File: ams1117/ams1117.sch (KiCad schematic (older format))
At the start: 8 parts, among them J1 PWR_IN, J2 PWR_OUT, J3 RAW, U1 AMS1117

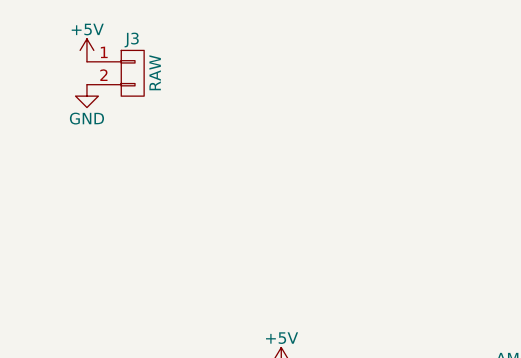
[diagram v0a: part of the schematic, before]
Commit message: 完成AMS1117降压模块PCB绘制
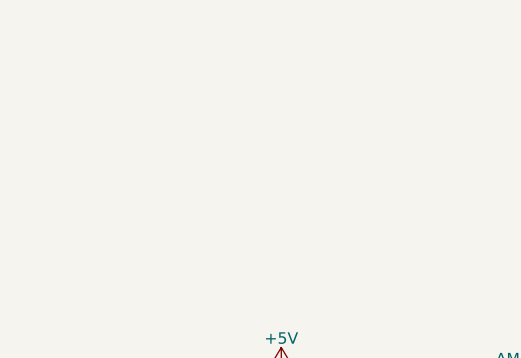
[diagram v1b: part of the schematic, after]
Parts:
- removed J3: RAW, symbol CONN_01X02
- C1, C4: footprint Capacitors_THT:CP_Radial_D5.0mm_P2.50mm -> Capacitors_SMD:CP_Elec_5x5.3
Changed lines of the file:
@@
 LIBS:contrib
 LIBS:valves
-LIBS:tmulin
 LIBS:ams1117-cache
 EELAYER 25 0
@@
 F 0 "C1" H 3175 3950 50  0000 L CNN
 F 1 "22uF" H 3175 3750 50  0000 L CNN
-F 2 "Capacitors_THT:CP_Radial_D5.0mm_P2.50mm" H 3188 3700 50  0001 C CNN
+F 2 "Capacitors_SMD:CP_Elec_5x5.3" H 3188 3700 50  0001 C CNN
 F 3 "" H 3150 3850 50  0001 C CNN
 	1    3150 3850
@@
 F 0 "C4" H 5425 3950 50  0000 L CNN
 F 1 "22uF" H 5425 3750 50  0000 L CNN
-F 2 "Capacitors_THT:CP_Radial_D5.0mm_P2.50mm" H 5438 3700 50  0001 C CNN
+F 2 "Capacitors_SMD:CP_Elec_5x5.3" H 5438 3700 50  0001 C CNN
 F 3 "" H 5400 3850 50  0001 C CNN
 	1    5400 3850
@@
 	1    0    0    -1
 $EndComp
-$Comp
-L CONN_01X02 J3
-U 1 1 5A055310
-P 2500 2100
-F 0 "J3" H 2500 2250 50  0000 C CNN
-F 1 "RAW" V 2600 2100 50  0000 C CNN
-F 2 "" H 2500 2100 50  0001 C CNN
-F 3 "" H 2500 2100 50  0001 C CNN
-	1    2500 2100
-	1    0    0    -1
-$EndComp
-$Comp
-L +5V #PWR010
-U 1 1 5A0553C5
-P 2300 2050
-F 0 "#PWR010" H 2300 1900 50  0001 C CNN
-F 1 "+5V" H 2300 2190 50  0000 C CNN
-F 2 "" H 2300 2050 50  0001 C CNN
-F 3 "" H 2300 2050 50  0001 C CNN
-	1    2300 2050
-	1    0    0    -1
-$EndComp
-$Comp
-L GND #PWR011
-U 1 1 5A0553F9
-P 2300 2150
-F 0 "#PWR011" H 2300 1900 50  0001 C CNN
-F 1 "GND" H 2300 2000 50  0000 C CNN
-F 2 "" H 2300 2150 50  0001 C CNN
-F 3 "" H 2300 2150 50  0001 C CNN
-	1    2300 2150
-	1    0    0    -1
-$EndComp
